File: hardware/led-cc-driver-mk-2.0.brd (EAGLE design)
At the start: 18 x 26 mm, 8 parts, among them Q1 2N3904, Q2 2N7000

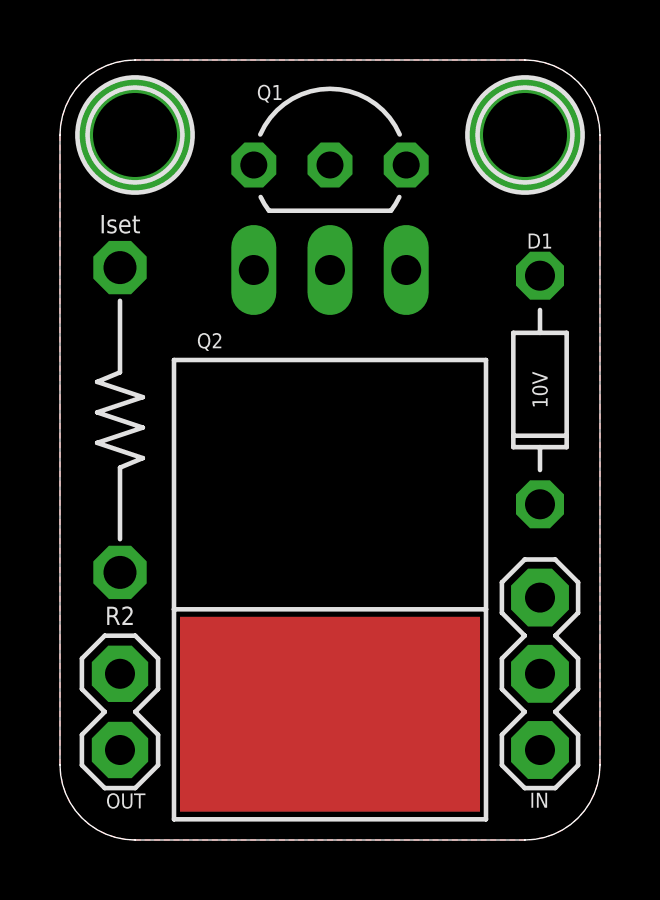
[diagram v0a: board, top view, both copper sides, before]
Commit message: layout for cc driver and some dicking around with the rgb one
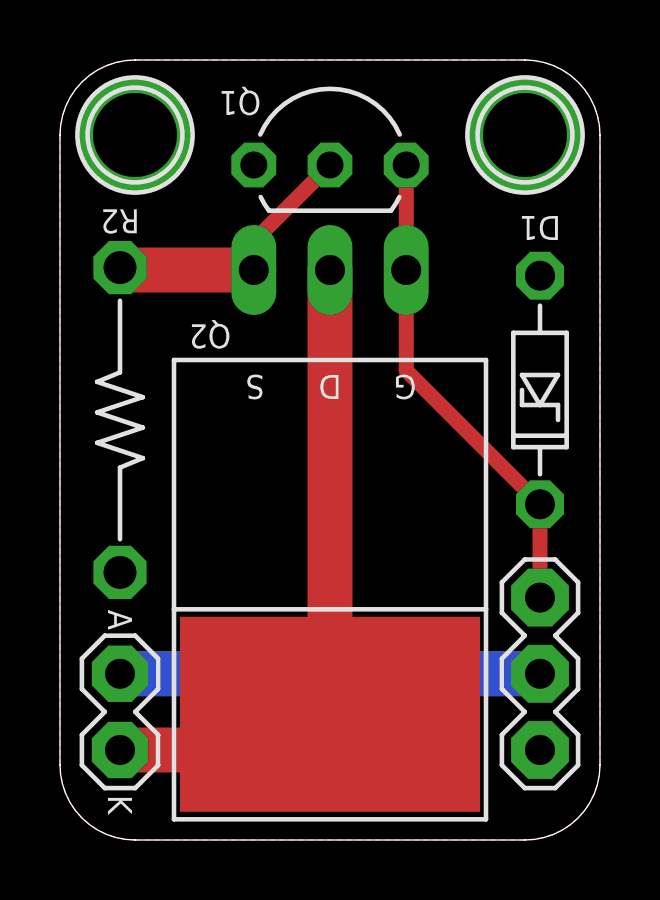
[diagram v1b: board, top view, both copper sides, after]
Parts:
- D1: device A_butts:DIODE-7.62MM -> A_butts:DIODE-ZENNER-7.62MM
- Q2: value 2N7000 -> FQP30N06L
- renumbered OUT to LED
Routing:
- net N$4: track 0.00 -> 22.3 mm
- net CTRL: track 0.00 -> 16.3 mm
- net VCC: track 0.00 -> 14.0 mm
- net N$1: track 0.00 -> 9.05 mm
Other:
- board text added: ">REVISION"
- board text added: "A"
- board text added: "Constant Current LED Driver"
- board text added: "D"
- board text added: "EN"
- board text added: "G"
- board text added: "GND"
- board text added: "K"
- board text added: "R1 = 0.5/I D1 = 10V Zener (opt)"
- board text added: "S"
- board text added: "VCC"
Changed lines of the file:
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@@
 <layer number="27" name="tValues" color="7" fill="1" visible="yes" active="yes"/>
 <layer number="28" name="bValues" color="7" fill="1" visible="yes" active="yes"/>
-<layer number="29" name="tStop" color="7" fill="3" visible="no" active="yes"/>
-<layer number="30" name="bStop" color="7" fill="6" visible="no" active="yes"/>
+<layer number="29" name="tStop" color="7" fill="3" visible="yes" active="yes"/>
+<layer number="30" name="bStop" color="7" fill="6" visible="yes" active="yes"/>
 <layer number="31" name="tCream" color="7" fill="4" visible="no" active="yes"/>
 <layer number="32" name="bCream" color="7" fill="5" visible="no" active="yes"/>
@@
 <wire x1="15.5" y1="26" x2="2.5" y2="26" width="0" layer="20"/>
 <wire x1="2.5" y1="26" x2="0" y2="23.5" width="0" layer="20" curve="90"/>
+<text x="14.5" y="5.5" size="0.8" layer="22" font="vector" ratio="12" rot="SMR270" align="bottom-center">VCC</text>
+<text x="14.5" y="3" size="0.8" layer="22" font="vector" ratio="12" rot="SMR270" align="bottom-center">GND</text>
+<text x="14.5" y="8" size="0.8" layer="22" font="vector" ratio="12" rot="SMR270" align="bottom-center">EN</text>
+<text x="3.5" y="5.5" size="0.8" layer="22" font="vector" ratio="12" rot="SMR90" align="bottom-center">A</text>
+<text x="3.5" y="3" size="0.8" layer="22" font="vector" ratio="12" rot="SMR90" align="bottom-center">K</text>
+<text x="2" y="7" size="0.8" layer="21" font="vector" ratio="12" rot="SR270" align="center-right">A</text>
+<text x="2" y="1.5" size="0.8" layer="21" font="vector" ratio="12" rot="SR270" align="center-left">K</text>
+<text x="9" y="15.5" size="0.8" layer="21" font="vector" ratio="12" rot="SR180" align="bottom-center">D</text>
+<text x="6.5" y="15.5" size="0.8" layer="21" font="vector" ratio="12" rot="SR180" align="bottom-center">S</text>
+<text x="11.5" y="15.5" size="0.8" layer="21" font="vector" ratio="12" rot="SR180" align="bottom-center">G</text>
+<text x="3.5" y="13" size="1" layer="22" font="vector" ratio="12" rot="SMR180" align="top-left">R1 = 0.5/I
+D1 = 10V Zener
+       (opt)</text>
+<text x="9" y="8.5" size="1" layer="22" font="vector" ratio="12" rot="SMR180" align="center">Constant
+Current
+LED
+Driver</text>
+<text x="9" y="24.5" size="1" layer="22" font="vector" ratio="12" rot="SMR180" align="center">&gt;REVISION</text>
 </plain>
 <attributes>
+<attribute name="REVISION" value="Rev 2.0"/>
 </attributes>
 <variantdefs>
@@
 <elements>
 <element name="Q1" library="A_butts" package="TO-92-AMMO" value="2N3904" x="9" y="22.5" smashed="yes">
-<attribute name="NAME" x="7" y="24.667" size="0.5" layer="25" font="vector" ratio="12" align="bottom-center"/>
-<attribute name="VALUE" x="9" y="23.651" size="0.5" layer="27" font="vector" ratio="12" rot="R180" align="top-center"/>
+<attribute name="NAME" x="6" y="24.167" size="0.8" layer="25" font="vector" ratio="12" rot="SR180" align="top-center"/>
+<attribute name="VALUE" x="9" y="23.849" size="0.5" layer="27" font="vector" ratio="12" rot="SR180" align="top-center"/>
 </element>
-<element name="Q2" library="A_butts" package="TO220-THERMPAD" value="2N7000" x="9" y="19" smashed="yes" rot="R180">
-<attribute name="NAME" x="5" y="16.89" size="0.5" layer="25" font="vector" ratio="10" rot="R180" align="bottom-center"/>
-<attribute name="VALUE" x="8.9" y="11.99" size="0.8" layer="27" font="vector" ratio="10" rot="R180" align="center"/>
+<element name="Q2" library="A_butts" package="TO220-THERMPAD" value="FQP30N06L" x="9" y="19" smashed="yes" rot="R180">
+<attribute name="NAME" x="5" y="16.39" size="0.8" layer="25" font="vector" ratio="12" rot="SR180" align="top-center"/>
+<attribute name="VALUE" x="8.9" y="11.99" size="0.8" layer="27" font="vector" ratio="10" rot="SR180" align="center"/>
 </element>
 <element name="R2" library="A_butts" package="RESISTOR-AXIAL-PTH-10.16MM" value="Iset" x="2" y="14" smashed="yes" rot="R90">
-<attribute name="NAME" x="2" y="7.777" size="0.6096" layer="25" font="vector" ratio="12" rot="R180" align="bottom-center"/>
-<attribute name="VALUE" x="2" y="20.223" size="0.6096" layer="21" font="vector" ratio="12" align="bottom-center"/>
+<attribute name="NAME" x="2" y="20.223" size="0.8" layer="25" font="vector" ratio="12" rot="SR180" align="top-center"/>
 </element>
 <element name="H1" library="A_butts" package="HOLE-#2" value="HOLE#2" x="2.5" y="23.5" smashed="yes"/>
-<element name="OUT" library="A_butts" package="1X02" value="M02PTH" x="2" y="3" smashed="yes" rot="R90">
-<attribute name="NAME" x="2.8462" y="1.5522" size="0.5" layer="25" font="vector" ratio="12" rot="R180"/>
+<element name="LED" library="A_butts" package="1X02" value="M02PTH" x="2" y="3" smashed="yes" rot="R90">
+<attribute name="NAME" x="0.95" y="4.27" size="0.7" layer="26" font="vector" ratio="12" rot="MR90" align="top-center"/>
 </element>
 <element name="H2" library="A_butts" package="HOLE-#2" value="HOLE#2" x="15.5" y="23.5" smashed="yes"/>
-<element name="IN" library="A_butts" package="1X03" value="M03PTH" x="16" y="3" smashed="yes" rot="R90">
-<attribute name="NAME" x="15.6538" y="1.0748" size="0.5" layer="25" font="vector" ratio="12"/>
-</element>
-<element name="D1" library="A_butts" package="DIODE-7.62MM" value="10V" x="16" y="15" smashed="yes" rot="R270">
-<attribute name="NAME" x="15.995" y="19.716" size="0.5" layer="25" font="vector" ratio="12" align="bottom-center"/>
-<attribute name="VALUE" x="16" y="15" size="0.508" layer="21" font="vector" ratio="12" rot="R270" align="center"/>
+<element name="IN" library="A_butts" package="1X03" value="M03PTH" x="16" y="3" smashed="yes" rot="R90"/>
+<element name="D1" library="A_butts" package="DIODE-ZENNER-7.62MM" value="10V" x="16" y="15" smashed="yes" rot="R270">
+<attribute name="NAME" x="16" y="20" size="0.8" layer="25" font="vector" ratio="12" rot="SR180" align="top-center"/>
 </element>
 </elements>
@@
 <contactref element="Q1" pad="2"/>
 <contactref element="Q2" pad="3"/>
-<wire x1="6.46" y1="19" x2="9" y2="22.5" width="0" layer="19" extent="1-1"/>
-<wire x1="2" y1="19.08" x2="6.46" y2="19" width="0" layer="19" extent="1-1"/>
+<wire x1="2" y1="19.08" x2="2.08" y2="19" width="1.5" layer="1"/>
+<wire x1="2.08" y1="19" x2="6.46" y2="19" width="1.5" layer="1"/>
+<wire x1="6.46" y1="19" x2="6.46" y2="19.96" width="0.5" layer="1"/>
+<wire x1="6.46" y1="19.96" x2="9" y2="22.5" width="0.5" layer="1"/>
 </signal>
 <signal name="VCC">
-<contactref element="OUT" pad="2"/>
+<contactref element="LED" pad="2"/>
 <contactref element="IN" pad="2"/>
-<wire x1="16" y1="5.54" x2="2" y2="5.54" width="0" layer="19" extent="1-16"/>
+<wire x1="2" y1="5.54" x2="16" y2="5.54" width="1.5" layer="16"/>
 </signal>
 <signal name="GND">
@@
 <contactref element="Q2" pad="1"/>
 <contactref element="D1" pad="K"/>
-<wire x1="11.54" y1="22.5" x2="11.54" y2="19" width="0" layer="19" extent="1-16"/>
-<wire x1="16" y1="11.19" x2="11.54" y2="19" width="0" layer="19" extent="1-1"/>
-<wire x1="16" y1="8.08" x2="16" y2="11.19" width="0" layer="19" extent="1-1"/>
+<wire x1="11.54" y1="22.5" x2="11.54" y2="19" width="0.5" layer="1"/>
+<wire x1="11.54" y1="19" x2="11.54" y2="15.65" width="0.5" layer="1"/>
+<wire x1="11.54" y1="15.65" x2="16" y2="11.19" width="0.5" layer="1"/>
+<wire x1="16" y1="8.08" x2="16" y2="11.19" width="0.5" layer="1"/>
 </signal>
 <signal name="N$4">
-<contactref element="OUT" pad="1"/>
+<contactref element="LED" pad="1"/>
 <contactref element="Q2" pad="2@1"/>
 <contactref element="Q2" pad="2@2"/>
-<wire x1="9" y1="19" x2="9" y2="4.19" width="0" layer="19" extent="1-16"/>
-<wire x1="2" y1="3" x2="9" y2="4.19" width="0" layer="19" extent="1-1"/>
+<wire x1="2" y1="3" x2="7.81" y2="3" width="1.5" layer="1"/>
+<wire x1="7.81" y1="3" x2="9" y2="4.19" width="0.8" layer="1"/>
+<wire x1="9" y1="19" x2="9" y2="4.19" width="1.5" layer="1"/>
 </signal>
 </signals>
 </board>
 </drawing>
+<compatibility>
+<note version="6.3" minversion="6.2.2" severity="warning">
+Since Version 6.2.2 text objects can contain more than one line,
+which will not be processed correctly with this version.
+</note>
+</compatibility>
 </eagle>
